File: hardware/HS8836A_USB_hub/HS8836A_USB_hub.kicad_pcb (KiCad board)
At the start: 2 copper layers, 25.2 x 99.4 mm, 13 parts, among them J2 USB_A, J3 USB_A, J4 USB_A, J5 USB_A, U1 HS8836A

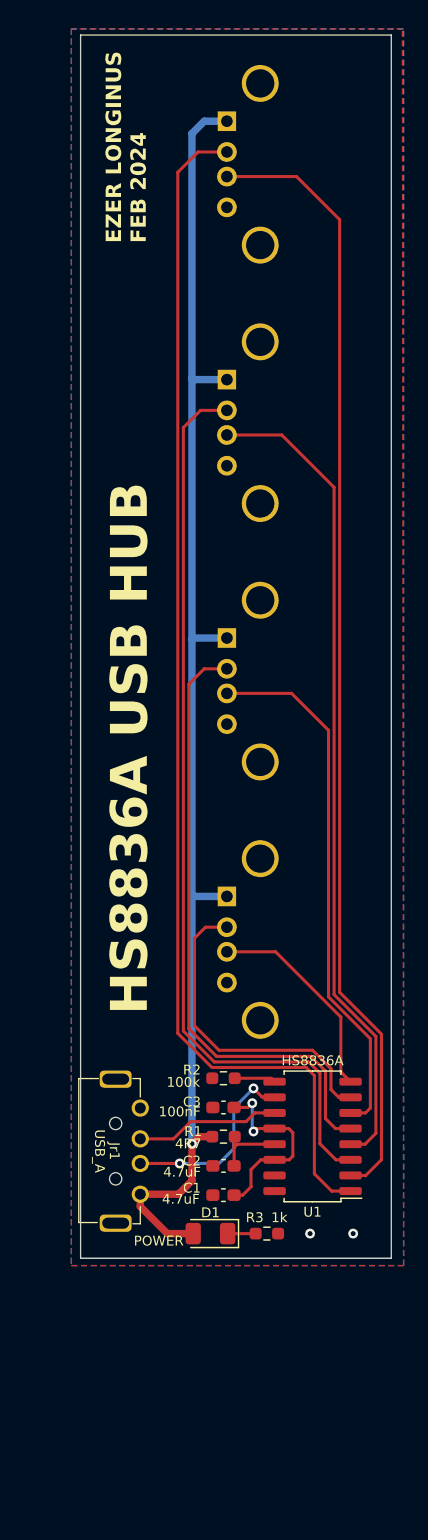
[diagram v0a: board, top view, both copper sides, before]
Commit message: Made the USB hub a little more universally applicable
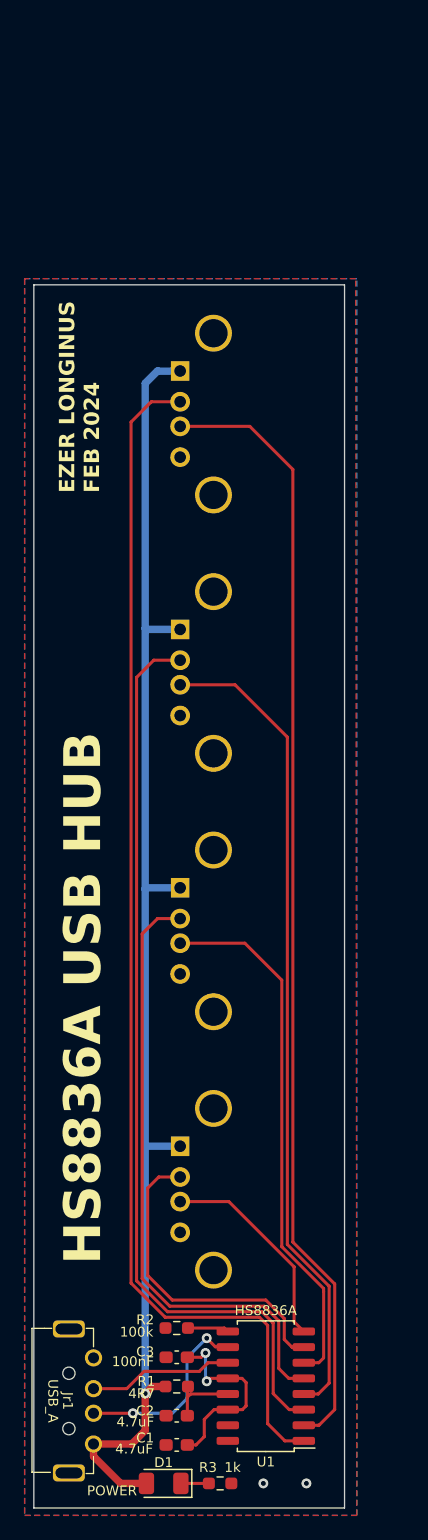
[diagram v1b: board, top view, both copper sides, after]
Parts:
- moved U1 20.7 mm to (152.8, 137.8)
- moved J2 20.7 mm to (145.8, 118.3)
- moved J3 20.7 mm to (145.8, 97.3)
- moved J4 20.7 mm to (145.8, 76.3)
- moved J5 20.7 mm to (145.8, 55.3)
- moved Jr1 20.7 mm to (138.8, 139.0)
- moved C1 20.7 mm to (145.6, 142.6)
- moved C2 20.7 mm to (145.6, 140.2)
- moved C3 20.7 mm to (145.6, 135.4)
- moved D1 20.7 mm to (144.5, 145.7)
- moved R1 20.7 mm to (145.6, 137.8)
- moved R2 20.7 mm to (145.6, 133.1)
- moved R3 20.7 mm to (149.1, 145.7)
